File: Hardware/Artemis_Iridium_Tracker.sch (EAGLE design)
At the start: 132 parts, among them J1 IRIDIUM_9603N, J14 CORTEX_DEBUG, J3 PTH, J8 uFL, J9 SMA-142-0711-821/826, Q1 DMG3414U-7, Q2 DMG3415U-7, U10 MCP73831, U2 LTC3225EDDB#TRMPBF, U3 ADM4210-1, U4 UBLOX_ZOE_M8-0-10, U5 AS179-92LF, U6 MS8607-02BA01, U7 ARTEMIS_MODULESMD, U8 AP3429A, U9 CH340E, Y1 32.768kHz, Y2 32.768kHz

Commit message: Updated the PCB - still work in progress!
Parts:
- removed BYP: JUMPER-SMT_2_NO_SILK, SparkFun-Jumpers:JUMPER-SMT_2_NO_SILK
- removed C32: 0.1uF, SparkFun-Capacitors:0.1UF-0603-25V-5%
- removed C33: 1nF, SparkFun-Capacitors:1.0NF/1000PF-0603-50V-10%
- removed C34: 4.7uF, SparkFun-Capacitors:4.7UF-0603-6.3V-(10%)
- removed D15: 3A/10V/280mV, SparkFun-DiscreteSemi:DIODE-SCHOTTKY-BAT60A
- removed F1: 6V/2A, SparkFun-Fuses:PPTC_6V2A
- removed J10: (no value), SparkFun-Connectors:USB_C2-LAYER
- removed J11: (no value), SparkFun-Connectors:CONN_05
- removed J12: (no value), SparkFun-Connectors:JST_2MM_MALE
- removed J8: uFL, microbuilder:ANTENNA_U.FL
- removed J9: SMA-142-0711-821/826, con-coax:SMA-142-0711-821/826
- removed JP3: JUMPER-SMT_2_NC_TRACE_SILK, SparkFun-Jumpers:JUMPER-SMT_2_NC_TRACE_SILK
- removed L3: 2.2μH, SparkFun-Coils:2.2μH-4X4-2.2μH-3A-45MOHM
- removed LOGO1: OSHW-LOGOMINI, SparkFun-Aesthetics:OSHW-LOGOMINI
- removed LOGO2: SFE_LOGO_NAME.1_INCH, SparkFun-Aesthetics:SFE_LOGO_NAME.1_INCH
- removed LOGO3: SFE_LOGO_NAME_FLAME.1_INCH, SparkFun-Aesthetics:SFE_LOGO_NAME_FLAME.1_INCH
- removed U10: MCP73831, SparkFun-IC-Power:MCP73831
- added !RESET, EN, GND: (no value), SparkFun-Connectors:CONN_01PTH_NO_SILK_YES_STOP
- added 3V3EN, JP2: JUMPER-SMT_2_NC_TRACE_SILK, SparkFun-Jumpers:JUMPER-SMT_2_NC_TRACE_SILK
- added 5V3, BUSV, RX(OUT), RX0, TX(IN), TX0: TEST-POINT3X5, SparkFun-Connectors:TEST-POINT3X5
- added C1: 10nF, SparkFun-Capacitors:10NF-0603-50V-10%
- added C7: 0.1uF, SparkFun-Capacitors:0.1UF-0603-25V-(+80/-20%)
- added D13: Yellow, SparkFun-LED:LED-YELLOW0603
- added I2C: PTH, SparkX:I2C_STANDARD_NO_SILK
- added L2: 2.2μH, SparkFun-Coils:2.2μH-4X4-2.2μH-3A-45MOHM
- added LOGO4: OSHW-LOGOMINI, SparkFun-Aesthetics:OSHW-LOGOMINI
- added Q3: DMG3415U-7, microbuilder:MOSFET-PWIDE
- added Q4: 2N2222, transistor:MMBT2222ALT1-NPN-SOT23-BEC
- added R2, R3: 1k, SparkFun-Resistors:1KOHM-0603-1/10W-1%
- added R20, R4: 5.1k, SparkFun-Resistors:5.1KOHM5.1KOHM-0603-1/10W-1%
- added R30: 10k, SparkFun-Resistors:10KOHM-0603-1/10W-1%
- added SPI: (no value), SparkFun-Connectors:CONN_07
- added U$29, U$30: SPARKX-LOGO4, SparkX:SPARKX-LOGO4
- added U1: CH340E_MSOP10, SparkFun-IC-Comms:CH340E_MSOP10
- BAT1, BAT2, BAT3: device SparkFun-Electromechanical:BATTERYKEYSTONE92 -> Iridium_9603_Beacon:BATTERYKEYSTONE82
- C17: value 1.0uF -> 4.7uF; device SparkFun-Capacitors:1.0UF-0603-16V-10% -> SparkFun-Capacitors:4.7UF-0603-6.3V-(10%)
- C29: value 10nF -> 1nF; device SparkFun-Capacitors:10NF-0603-50V-10% -> SparkFun-Capacitors:1.0NF/1000PF-0603-50V-10%
- C30: device SparkFun-Capacitors:0.1UF-0603-25V-(+80/-20%) -> SparkFun-Capacitors:0.1UF-0603-25V-5%
- D7: value Yellow -> GREEN; device SparkFun-LED:LED-YELLOW0603 -> SparkFun-LED:LED-GREEN0603
- D8: value GREEN -> 3A/10V/280mV; device SparkFun-LED:LED-GREEN0603 -> SparkFun-DiscreteSemi:DIODE-SCHOTTKY-BAT60A
- J2: value (none) -> USB-C; device SparkFun-Connectors:CONN_021X02_NO_SILK -> SparkFun-Connectors:USB_C2-LAYER
- J3: value PTH -> (none); device SparkX:I2C_STANDARD_NO_SILK -> SparkFun-Connectors:JST_2MM_MALE
- J5: device SparkFun-Connectors:CONN_01PTH_NO_SILK_YES_STOP -> SparkFun-Connectors:JST_2MM_MALE
- J6: value (none) -> uFL; device SparkFun-Connectors:CONN_01PTH_NO_SILK_YES_STOP -> microbuilder:ANTENNA_U.FL
- J7: value (none) -> SMA-142-0711-821/826; device SparkFun-Connectors:CONN_01PTH_NO_SILK_YES_STOP -> con-coax:SMA-142-0711-821/826
- R22: value 1k -> 10k; device SparkFun-Resistors:1KOHM-0603-1/10W-1% -> SparkFun-Resistors:10KOHM-0603-1/10W-1%
- R23: value 330 -> 10k; device SparkFun-Resistors:330OHM-0603-1/10W-1% -> SparkFun-Resistors:10KOHM-0603-1/10W-1%
- R24: value 5.1k -> 20k; device SparkFun-Resistors:5.1KOHM5.1KOHM-0603-1/10W-1% -> SparkFun-Resistors:20KOHM-0603-1/10W-1%
- R25: value 5.1k -> 1k; device SparkFun-Resistors:5.1KOHM5.1KOHM-0603-1/10W-1% -> SparkFun-Resistors:1KOHM-0603-1/10W-1%
- U9: value CH340E -> MCP73831; device SparkFun-IC-Comms:CH340E_MSOP10 -> SparkFun-IC-Power:MCP73831
- renumbered C35 to C8, J14 to DEBUG, J16 to QWIIC, S2 to S1, Y1 to X2, Y2 to X1
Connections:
- removed net ARTEMIS_SHLD: J10.SHLD
- removed net CC1: J10.CC1, R25.2
- removed net CC2: J10.CC2, R24.2
- removed net D+1: J10.D+, U9.UD+
- removed net D-1: J10.D-, U9.UD-
- removed net N$38 (its old number): BYP.1, F1.1, J10.VBUS
- new net CC3: J2.CC2, R4.2
- new net CC4: J2.CC1, R20.2
- new net D+2: J2.D+, U1.UD+
- new net D-2: J2.D-, U1.UD-
- new net N$22: D7.A, R3.1
- new net N$34: D13.A, R2.1
- new net N$46: Q3.D, R24.1
- new net N$47: Q4.B, R25.2
- new net SHLD: J2.SHLD
- net 3.3V: now also C1.1, C12.1, C7.1, I2C.VCC, JP2.2, L2.2, R2.2, R3.2, SPI.7, U1.V3, U1.VCC, U6.VDD; no longer C17.1, C29.1, C30.1, J11.5, L3.2, R1.2, R22.2, R23.2, U9.V3, U9.VCC
- net 3V3SW: no longer C12.1, J3.VCC, U6.VDD
- net ANTENNA: now also J7.1; no longer J9.1
- net ARTEMIS_!RESET: now also !RESET.1, C29.1; no longer C33.1, J5.1
- net ARTEMIS_!RTS!: now also C30.1, U1.!RTS; no longer C32.1, U9.!RTS
- net ARTEMIS_BOOT: now also C30.2; no longer C32.2
- net ARTEMIS_D10: now also U4.P1014; no longer U4.P1015
- net ARTEMIS_D13: now also BUSV.1, R23.1, R24.2
- net ARTEMIS_D24: now also TX(IN).1
- net ARTEMIS_D25: now also RX(OUT).1
- net ARTEMIS_D34: now also R25.1, R30.1
- net ARTEMIS_D35: now also SPI.5
- net ARTEMIS_D4: now also SPI.6
- net ARTEMIS_D42: no longer J6.1
- net ARTEMIS_D5_SCK: now also SPI.4; no longer J11.4
- net ARTEMIS_D6_MISO: now also SPI.3; no longer J11.3
- net ARTEMIS_D7_MOSI: now also SPI.2; no longer J11.2
- net ARTEMIS_D8_SCL: now also I2C.SCL; no longer J3.SCL
- net ARTEMIS_D9_SDA: now also I2C.SDA; no longer J3.SDA
- net ARTEMIS_RX0: now also D13.C, RX0.1, U1.TXO; no longer D7.C, U9.TXO
- net ARTEMIS_TX0: now also D7.C, TX0.1, U1.RXI; no longer D8.C, U9.RXI
- net EXT_PWR: now also 5V3.1; no longer J7.1
- net GND: now also C1.2, C7.2, GND.1, I2C.GND, J2.GND, J3.-, J5.-, J6.GND@0, J6.GND@1, J7.2, Q4.E, R20.1, R23.2, R30.2, R4.1, SPI.1, U1.GND, U9.VSS; no longer C30.2, C33.2, C34.2, J10.GND, J11.1, J12.-, J2.1, J3.GND, J8.GND@0, J8.GND@1, J9.2, R24.1, R25.1, U10.VSS, U9.GND
- net IRIDIUM: now also J6.SIGNAL; no longer J8.SIGNAL
- net N$23: now also D1.A; no longer JP3.2
- net N$3: now also JP2.1, R1.2; no longer D1.A, JP3.1
- net N$33: now also L2.1; no longer L3.1
- net N$36: now also 3V3EN.2, EN.1, U8.EN; no longer D8.A, R23.1
- net N$37: now also Q3.G, Q4.C; no longer D7.A
- net N$39: now also U9.PROG; no longer U10.PROG
- net N$41: now also U9.STAT; no longer U10.STAT
- net N$42: now also J3.+
- net N$45: now also D8.C; no longer D15.C
- net VIN: now also 3V3EN.1, Q3.S, R22.2; no longer U8.EN
- net V_BATT: now also D8.A, J5.+, U9.VBAT; no longer D15.A, J12.+, J2.2, U10.VBAT
- net V_USB: now also C17.1, J2.VBUS, U9.VIN; no longer BYP.2, C34.1, F1.2, U10.VIN
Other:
- note added: "3 x AAA Energiser Ultimate Lithium in Keystone Electronics 82 clips"
- note added: "Back-Up Battery"
- note added: "Bus Voltage Measurement"
- note removed: "3 x AA Energiser Ultimate Lithium in Keystone Electronics 92 clips"
- note removed: "Battery"
- note removed: "SPI"
- note removed: "This is the bypass jumper Close only if you know what you're doing."
- note removed: "WAKE"
- moved on the sheet: B1, BAT1, BAT2, BAT3, C24, C25, C26, C27, C28, D10, D14, D5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

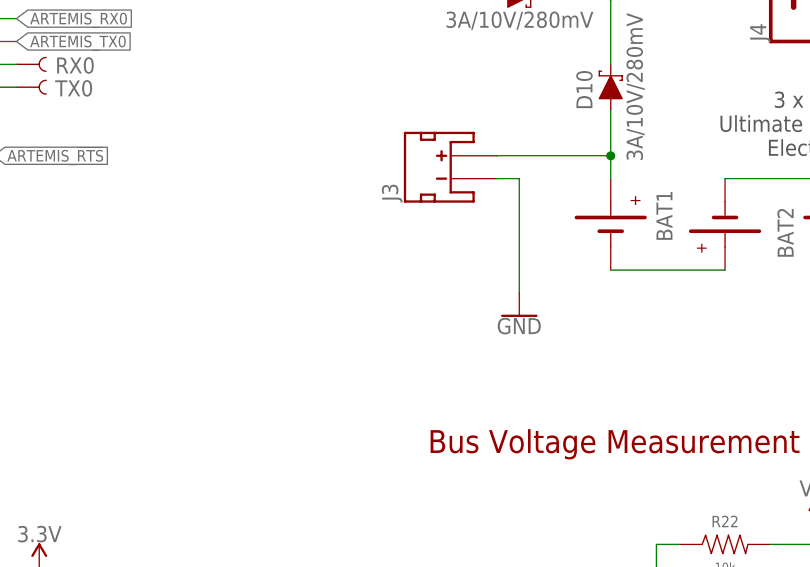
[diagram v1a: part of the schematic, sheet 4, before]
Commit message: PCB is routed - grounding needs checking
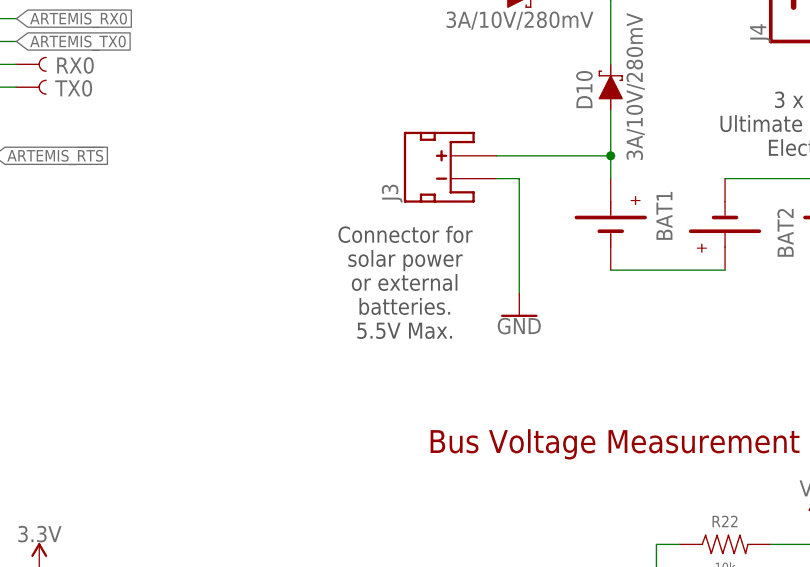
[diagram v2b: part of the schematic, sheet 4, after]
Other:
- note added: "Connector for solar power or external batteries. 5.5V Max."
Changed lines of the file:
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@@
 Electronics 82 clips</text>
 <text x="172.72" y="101.6" size="2.54" layer="94" font="vector" ratio="15">Bus Voltage Measurement</text>
+<text x="170.18" y="114.3" size="1.778" layer="97" font="vector" align="bottom-center">Connector for
+solar power
+or external
+batteries.
+5.5V Max.</text>
 </plain>
 <instances>

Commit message: Final PCB tweaks - ready for prototyping!
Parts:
- added U10: MCP111T-240E/TT, Microchip-MCP11:MCP111T-270E/TT
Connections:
- net 3.3V: now also U10.VDD
- net ARTEMIS_!RESET: now also U10.VOUT
- net GND: now also U10.VSS
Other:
- moved on the sheet: DEBUG, QWIIC

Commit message: Tweaked the SMA position
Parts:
- J7: value SMA-142-0711-821/826 -> SMA-; device con-coax:SMA-142-0711-821/826 -> Qwiic_Iridium_9603N:SMA-
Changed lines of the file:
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@@
 <part name="Q2" library="microbuilder" deviceset="MOSFET-P" device="WIDE" value="DMG3415U-7 "/>
 <part name="J6" library="microbuilder" deviceset="ANTENNA_U.FL" device="" value="uFL"/>
-<part name="J7" library="con-coax" library_urn="urn:adsk.eagle:library:133" deviceset="SMA-" device="142-0711-821/826" package3d_urn="urn:adsk.eagle:package:6224/1"/>
+<part name="J7" library="Qwiic_Iridium_9603N" deviceset="SMA-" device=""/>
 <part name="U5" library="SamacSys_Parts" deviceset="AS179-92LF" device=""/>
 <part name="C14" library="SparkFun-Capacitors" library_urn="urn:adsk.eagle:library:510" deviceset="100PF" device="-0603-50V-5%" package3d_urn="urn:adsk.eagle:package:37414/1" value="100pF"/>

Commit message: Substantial update for V2 (X01) of the PCB
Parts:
- removed BAT1, BAT2, BAT3: (no value), Iridium_9603_Beacon:BATTERYKEYSTONE82
- removed C26: 22pF, SparkFun-Capacitors:22PF-0603-50V-5%
- removed L2: 2.2μH, SparkFun-Coils:2.2μH-4X4-2.2μH-3A-45MOHM
- removed R18: 453k, SparkFun-Resistors:453KOHM-0603-1/10W-1%
- removed R19: 100k, SparkFun-Resistors:100KOHM-0603-1/10W-1%
- removed U8: AP3429A, SparkFun-IC-Power:AP3429/A
- added U11: 3.3V, SparkFun-IC-Power:V_REG_AP2112K-3.3V
- C24: value 22uF -> 1.0uF; device SparkFun-Capacitors:22UF-0603-6.3V-20% -> SparkFun-Capacitors:1.0UF-0603-16V-10%
- D10, D11, D12, D14, D8: value 3A/10V/280mV -> 0.5A/40V/420mV; device SparkFun-DiscreteSemi:DIODE-SCHOTTKY-BAT60A -> SparkFun-DiscreteSemi:DIODE-SCHOTTKY-PMEG4005EJ
- J7: value SMA- -> ANTENNA-GROUNDEDEDGE_SMA; device Qwiic_Iridium_9603N:SMA- -> Qwiic_Iridium_9603N:ANTENNA-GROUNDEDEDGE_SMA
- renumbered BUSV to VIN/3
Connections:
- net N$45 renamed VBUS
- removed net ARTEMIS_D0: U7.(SLSCK/SLSCL/CLKOUT)D0
- removed net ARTEMIS_D1: U7.(SLMOSI/SLSDA)D1
- removed net ARTEMIS_D11: U7.~AD11(PDMDATA)
- removed net ARTEMIS_D12: U7.~AD12(PDMCLK/TX1)
- removed net ARTEMIS_D14_TX1: U7.(ADCD1P/TX1/PDMCLK)D14
- removed net ARTEMIS_D15_RX1: U7.(ADCD1N/RX1/PDMDATA)D15
- removed net ARTEMIS_D16: U7.AD16(TRIG0/SCCRST)
- removed net ARTEMIS_D2: U7.(SLMISO)D2
- removed net ARTEMIS_D23: U7.(I2SWCLK/CMPOUT)~D23
- removed net ARTEMIS_D29: U7.~AD29(PDMDATA)
- removed net ARTEMIS_D3: U7.(SLNCE/I2SWCLK)D3
- removed net ARTEMIS_D31: U7.~AD31(SCCCLK)
- removed net ARTEMIS_D32: U7.~AD32(SCCIO)
- removed net ARTEMIS_D36_PDMDATA: U7.(RX1/TRIG1/PDMDATA)D36
- removed net ARTEMIS_D37_PDMCLK: U7.(TX1/PDMCLK/SCCIO)~D37
- removed net ARTEMIS_D38: U7.(MOSI3/RX1)D38
- removed net ARTEMIS_D42: U7.(SCL3/SCK3/TX1)~D42
- removed net ARTEMIS_D43: U7.(SDA3/MISO3/RX1)~D43
- removed net ARTEMIS_D44: U7.(MOSI4)~D44
- removed net ARTEMIS_D45: U7.(SWO/I2SDAT/PDMDATA)~D45
- removed net N$33: L2.1, U8.LX
- removed net N$34: D13.A, R2.1
- removed net N$38: BAT1.-, BAT2.+
- removed net N$42: BAT1.+, D10.A, J3.+
- removed net N$43: BAT2.-, BAT3.+
- new net V_AAA: D10.A, J3.+
- net 3.3V: now also D13.A, D7.A, R1.2, U11.OUT; no longer C26.1, JP2.2, L2.2, R18.2, R2.2, R3.2
- net ANTENNA: now also J7.SIGNAL; no longer J7.1
- net ARTEMIS_RX0: now also R2.1; no longer D13.C
- net ARTEMIS_TX0: now also R3.1; no longer D7.C
- net GND: now also J7.GND, U11.GND; no longer BAT3.-, J7.2, R19.1, U8.GND
- net N$22: now also D13.C, R2.2; no longer D7.A, R3.1
- net N$23: now also JP2.1; no longer R1.1
- net N$3: now also JP2.2, R1.1; no longer JP2.1, R1.2
- net N$32: now also D7.C, R3.2; no longer C26.2, R18.1, R19.2, U8.FB
- net N$36: now also U11.EN; no longer U8.EN
- net VIN: now also U11.IN; no longer U8.VIN
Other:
- note added: "3.3V @ 600mA Iq = 50uA"
- note added: "Connector for solar power or 3 x AA/AAA 6V Max"
- note added: "Reset Supervisor: Select On Test (May be required for solar power)"
- note added: "V2"
- note removed: "3 x AAA Energiser Ultimate Lithium in Keystone Electronics 82 clips"
- note removed: "Connector for solar power or external batteries. 5.5V Max."
- note removed: "DC-DC Buck: 3.3V@2A"
- note removed: "V1"
- moved on the sheet: 3V3EN, C21, C25, C27, C28, C29, C30, C31, D1, D13, D2, D3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

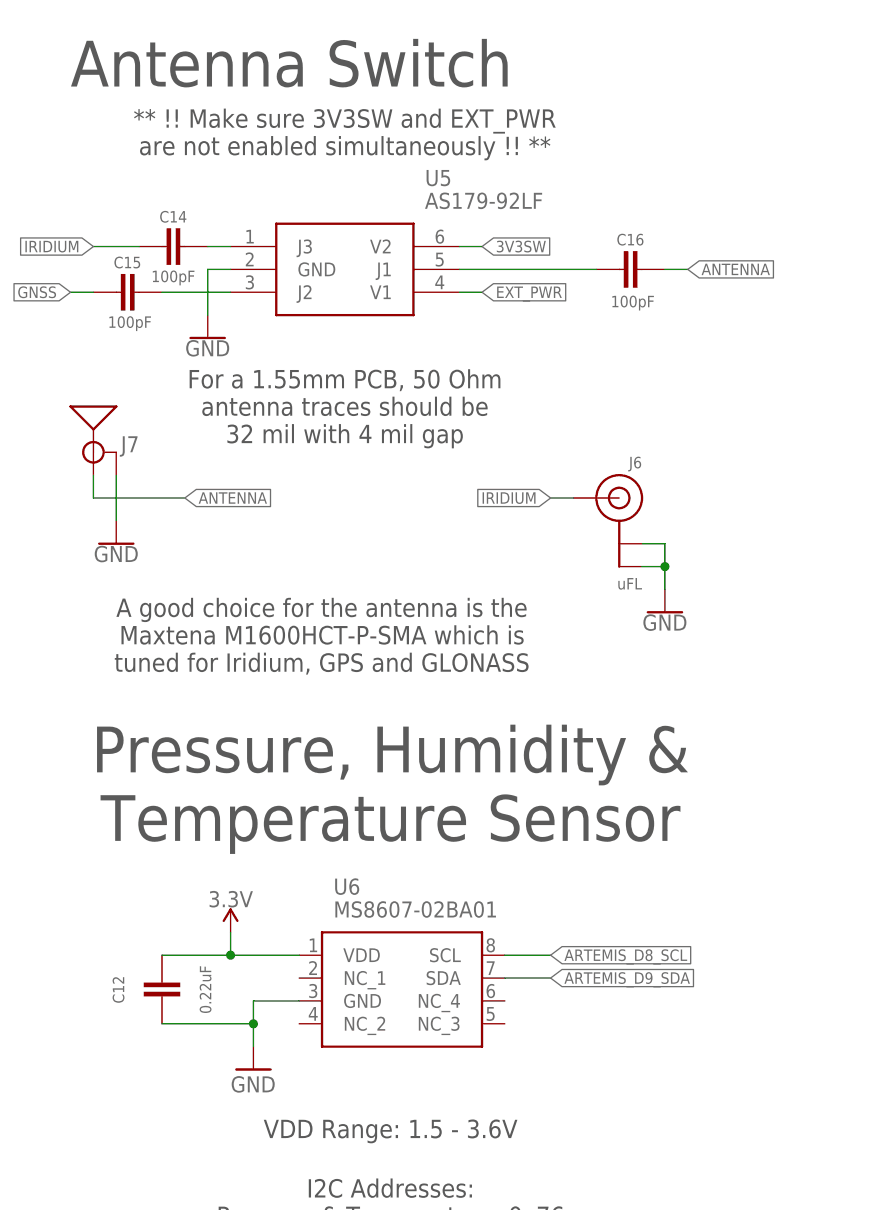
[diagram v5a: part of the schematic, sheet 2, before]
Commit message: Updated the PCB - tidied up the libraries
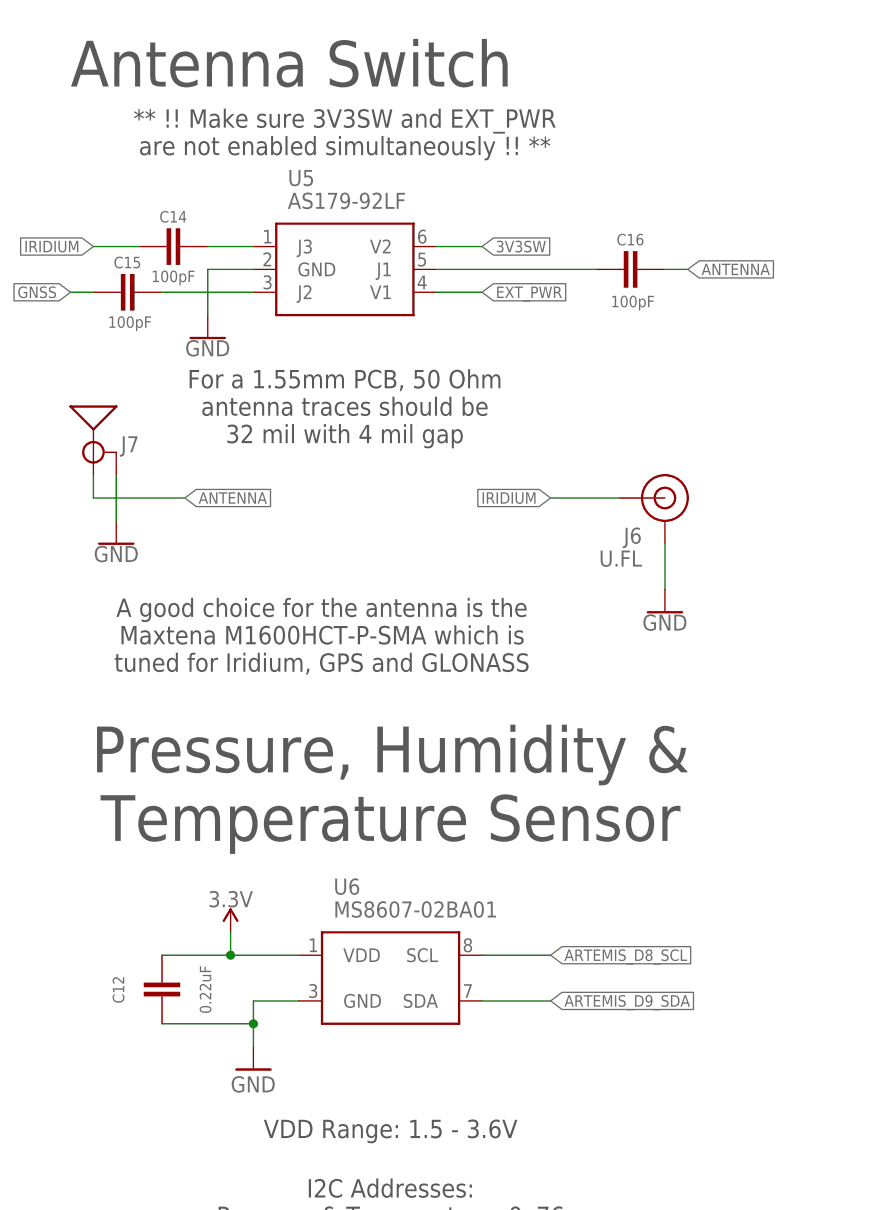
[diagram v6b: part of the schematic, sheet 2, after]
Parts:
- removed U$29, U$30: SPARKX-LOGO4, SparkX:SPARKX-LOGO4
- removed U11: 3.3V, SparkFun-IC-Power:V_REG_AP2112K-3.3V
- added SPARKX1, SPARKX2: SPARKX-LOGO4, SparkX:SPARKX-LOGO4
- added U8: V_SUPERVISORBD48K24G-TL, New_Parts:V_SUPERVISORBD48K24G-TL
- C10, C3: device SparkFun-Capacitors:1.0UF-0603-16V-10% -> SparkFun-Capacitors:1.0UF-0603-16V-10%-X7R
- I2C: device SparkX:I2C_STANDARD_NO_SILK -> SparkFun-Connectors:I2C_STANDARD_NO_SILK
- J1: device Qwiic_Iridium_9603N:IRIDIUM_9603N -> New_Parts:IRIDIUM_9603N
- J6: value uFL -> U.FL; device microbuilder:ANTENNA_U.FL -> SparkFun-Connectors:U.FL2PIN
- J7: device Qwiic_Iridium_9603N:ANTENNA-GROUNDEDEDGE_SMA -> SparkFun-RF:ANTENNA-GROUNDEDEDGE_SMA
- JP1: value JUMPER-PAD-3-2OF3_NC_BY_TRACE_LARGE -> JUMPER-SMT_3_1-NC_TRACE_SILK; device Qwiic_Iridium_9603N:JUMPER-PAD-3-2OF3_NC_BY_TRACE_LARGE -> SparkFun-Jumpers:JUMPER-SMT_3_1-NC_TRACE_SILK
- JP10, JP11, JP12, JP9: device SparkFun:STAND-OFF -> SparkFun-Hardware:STAND-OFF
- JP13, JP14, JP7, JP8: value FIDUCIALUFIDUCIAL -> FIDUCIAL1X2; device SparkFun:FIDUCIALUFIDUCIAL -> SparkFun-Aesthetics:FIDUCIAL1X2
- Q1: device DMG3414U-7:DMG3414U-7 -> New_Parts:DMG3414U-7
- Q2, Q3: device microbuilder:MOSFET-PWIDE -> New_Parts:DMG3415U
- Q4: value 2N2222 -> 600mA/40V; device transistor:MMBT2222ALT1-NPN-SOT23-BEC -> SparkFun-DiscreteSemi:TRANS_NPN-MMBT2222AL
- QWIIC: value (none) -> QWIIC_RIGHT_ANGLE
- R9: value 0.012 Ohm -> 0.012R; device SparkFun-Resistors:RESISTOR0603 -> New_Parts:RESISTOR_0603_12MILLIOHM0603
- SPI: device SparkFun-Connectors:CONN_07 -> SparkFun-Connectors:CONN_07NO_SILK
- U10: value MCP111T-240E/TT -> 3.3V; device Microchip-MCP11:MCP111T-270E/TT -> SparkFun-IC-Power:V_REG_AP2112K-3.3V; MPN MCP111T-240E/TT -> (none)
- U2: device Qwiic_Iridium_9603N:LTC3225EDDB-TRMPBFDFN300X200-10L -> New_Parts:LTC3225EDDB-TRMPBFDFN300X200-10L
- U3: device ADM4210:ADM4210-1 -> New_Parts:ADM4210-1
- U5: device SamacSys_Parts:AS179-92LF -> New_Parts:AS179-92LF
- U6: device SamacSys_Parts:MS8607-02BA01 -> New_Parts:MS8607-02BA01
- renumbered RX(OUT) to RX1, TX(IN) to TX1
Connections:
- removed net SHLD: J2.SHLD
- net 3.3V: now also I2C.2, U10.OUT, U8.VCC; no longer I2C.VCC, U10.VDD, U11.OUT
- net ARTEMIS_!RESET: now also U8.VOUT; no longer U10.VOUT
- net ARTEMIS_D8_SCL: now also I2C.4; no longer I2C.SCL
- net ARTEMIS_D9_SDA: now also I2C.3; no longer I2C.SDA
- net GND: now also I2C.1, J6.GND, U10.GND, U8.GND; no longer I2C.GND, J6.GND@0, J6.GND@1, U10.VSS, U11.GND
- net N$36: now also U10.EN; no longer U11.EN
- net VIN: now also U10.IN; no longer U11.IN
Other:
- note added: "2.4V Reset Supervisor (Ensures a clean start on solar power)"
- note removed: "Reset Supervisor: Select On Test (May be required for solar power)"
- moved on the sheet: DEBUG

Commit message: Updated the PCB and the examples README
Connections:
- net N$31 renamed XTALI
- net N$7 renamed XTALO
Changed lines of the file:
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@@
 </segment>
 </net>
-<net name="N$7" class="0">
+<net name="XTALO" class="0">
 <segment>
 <wire x1="55.88" y1="109.22" x2="38.1" y2="109.22" width="0.1524" layer="91"/>
@@
 </segment>
 </net>
-<net name="N$31" class="0">
+<net name="XTALI" class="0">
 <segment>
 <pinref part="X1" gate="G$1" pin="1"/>
